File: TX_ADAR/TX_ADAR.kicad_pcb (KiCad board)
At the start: 4 copper layers, 68.5 x 197.6 mm, 73 parts, among them IC1 REG1117A-1.8, IC2 REG1117A-2.5, J1 Conn_Coaxial, J10 Conn_Coaxial, J11 RJ45_LED_Shielded, J12 RJ45_LED_Shielded, J16 RJ45_LED_Shielded, J2 Conn_Coaxial, J21 Conn_01x04, J3 Conn_Coaxial, J4 Conn_Coaxial, J5 Conn_Coaxial, J6 Conn_Coaxial, J7 Conn_Coaxial, J8 Conn_Coaxial, J9 Conn_Coaxial, SW1 SW_SPDT, SW2 SW_SPDT, SW3 SW_SPDT, SW9 SW_SPDT, U10 TXB0101DBV, U11 TXB0101DBV, U14 TXB0101DBV, U15 TXB0101DBV, U16 TXB0101DBV, U17 TXB0101DBV, U18 TXB0101DBV, U19 TXB0101DBV, U2 ADAR2001ACCZ

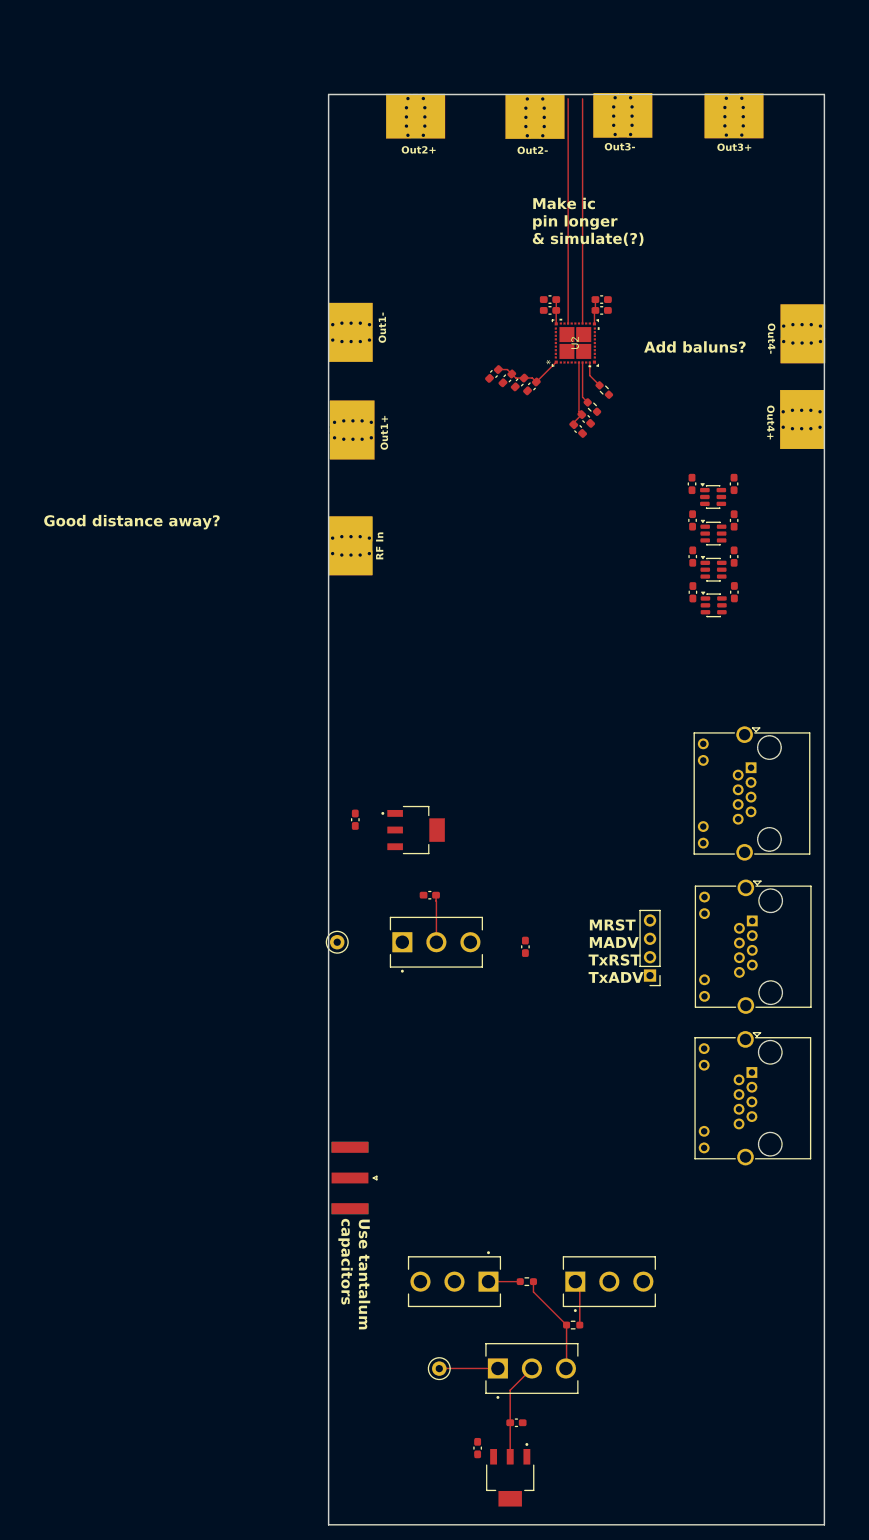
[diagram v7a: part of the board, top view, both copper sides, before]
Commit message: Fixed footprint and meddled with the layout
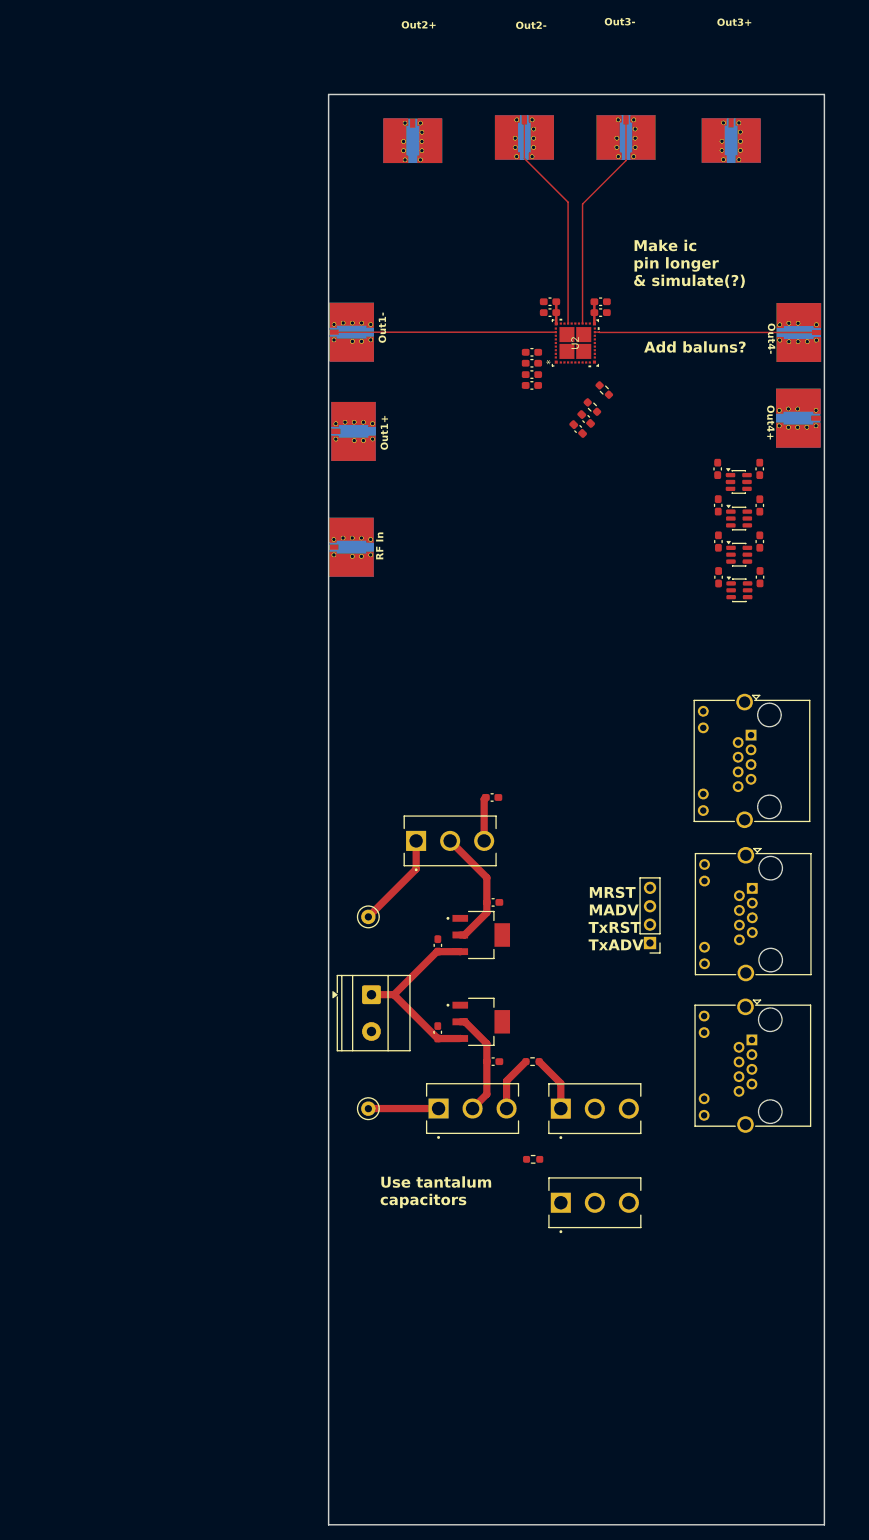
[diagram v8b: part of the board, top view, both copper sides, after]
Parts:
- J1: value Conn_Coaxial -> Screw_Terminal_01x02; footprint Connector_Coaxial:SMA_Amphenol_132289_EdgeMount -> TerminalBlock_Phoenix:TerminalBlock_Phoenix_MKDS-1,5-2-5.08_1x02_P5.08mm_Horizontal
- moved IC1 63.1 mm to (122.5, 117.0), turned to 0 degrees
- moved C3 57.7 mm to (116.5, 118.4)
- moved C1 50.0 mm to (124.1, 122.5)
- moved TP3 37.2 mm to (106.9, 129.0)
- moved SW2 36.8 mm to (121.3, 129.0)
- moved R2 36.8 mm to (129.6, 122.5)
- moved J1 25.5 mm to (107.3, 113.3), turned to -90 degrees
- moved SW1 24.0 mm to (138.2, 129.0)
- moved SW3 22.3 mm to (138.2, 142.0), turned to 90 degrees
- moved C32 21.1 mm to (124.0, 86.0), turned to 0 degrees
- moved C2 20.8 mm to (116.5, 106.4), turned to 90 degrees
- moved IC2 17.1 mm to (122.5, 105.0)
- moved R3 16.9 mm to (129.7, 136.0), turned to 180 degrees
- moved SW9 14.1 mm to (118.2, 92.0)
- moved C4 8.80 mm to (124.1, 100.5), turned to 0 degrees
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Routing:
- net /RFOut1-: track 0.00 -> 30.7 mm
- net /RFOut4-: track 0.00 -> 30.6 mm
- net +5V: track 0.00 -> 26.4 mm
- net +1V8: track 23.7 -> 8.10 mm
- net Net-(SW9-A): track 0.00 -> 13.2 mm
- net Net-(IC2-VOUT): track 6.52 -> 17.0 mm
- net /TxADV: track 5.81 -> 0.00 mm
- net +2V5: track 16.7 -> 12.3 mm
- net Net-(SW3-A): track 4.39 -> 0.00 mm
- net /MADV: track 3.72 -> 0.00 mm
- net Net-(SW2-A): track 8.11 -> 9.71 mm
- net Net-(SW1-A): track 6.25 -> 7.74 mm
- net Net-(IC1-VOUT): track 13.4 -> 14.7 mm
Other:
- board text removed: "Good distance away?"
